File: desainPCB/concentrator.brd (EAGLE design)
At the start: 191.8 x 77.1 mm, 23 parts, among them M1 ARDUINO-PRO-MINI-5.0V, M2 ARDUINO-PRO-MINI-5.0V, M3 ARDUINO-PRO-MINI-5.0V, M4 ARDUINO-PRO-MINI-5.0V

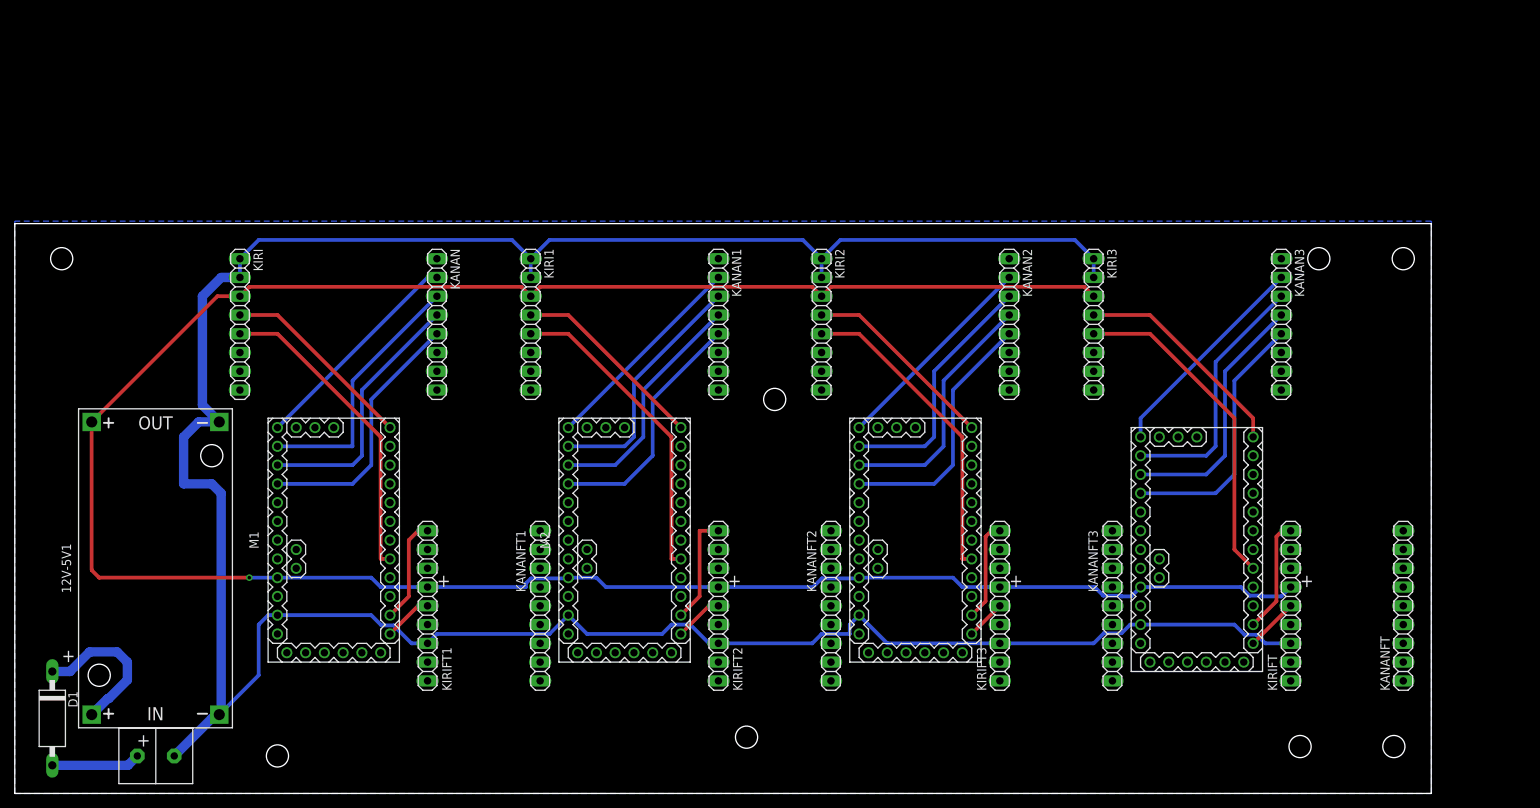
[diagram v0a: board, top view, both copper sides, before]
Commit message: new sensor suhu
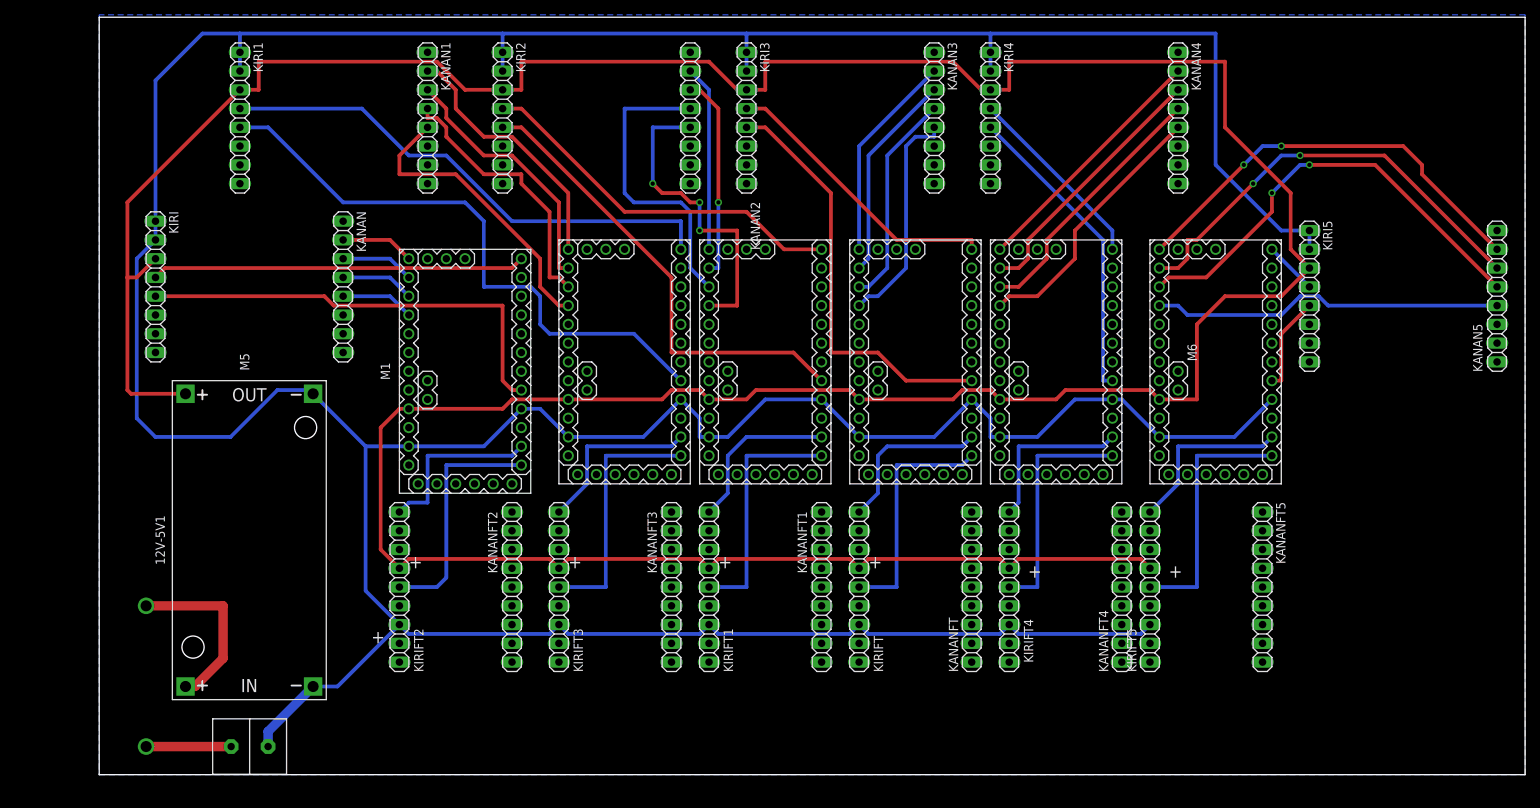
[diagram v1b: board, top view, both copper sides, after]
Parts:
- removed D1: 1N5060GP, diode:DO15-12
- added KANAN4, KANAN5, KIRI4, KIRI5: (no value), pinhead:1X08
- added KANANFT4, KANANFT5, KIRIFT4, KIRIFT5: (no value), pinhead:1X09
- added M5, M6: ARDUINO-PRO-MINI-5.0V, diy-modules:ARDUINO-PRO-MINI
- moved KANANFT3 59.7 mm to (88.9, 27.9)
- moved KIRIFT3 59.7 mm to (73.7, 27.9)
- moved KANANFT 58.5 mm to (129.5, 27.9)
- moved KIRIFT 58.5 mm to (114.3, 27.9)
- moved KIRI3 54.7 mm to (99.1, 91.4)
- moved KANAN3 54.7 mm to (124.5, 91.4)
- moved KANAN2 51.4 mm to (91.4, 91.4)
- moved KIRI2 51.4 mm to (66.0, 91.4)
- moved KANAN1 48.3 mm to (55.9, 91.4)
- moved KIRI1 48.3 mm to (30.5, 91.4)
- moved M4 45.8 mm to (121.9, 58.4)
- moved KIRIFT2 43.3 mm to (52.1, 27.9)
- moved KANANFT2 43.3 mm to (67.3, 27.9)
- moved KIRIFT1 38.2 mm to (94.0, 27.9)
- moved KANANFT1 38.2 mm to (109.2, 27.9)
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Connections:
- removed net 10: KANAN.2, KANAN1.2, KANAN2.2, KANAN3.2, M1.J6.12, M2.J6.12, M3.J6.12, M4.J6.12
- removed net 11: KANAN.3, KANAN1.3, KANAN2.3, KANAN3.3, M1.J6.11, M2.J6.11, M3.J6.11, M4.J6.11
- removed net 12: KANAN.4, KANAN1.4, KANAN2.4, KANAN3.4, M1.J6.10, M2.J6.10, M3.J6.10, M4.J6.10
- removed net 13: KANAN.5, KANAN1.5, KANAN2.5, KANAN3.5, M1.J6.9, M2.J6.9, M3.J6.9, M4.J6.9
- removed net 2: KIRI.5, KIRI1.5, KIRI2.5, KIRI3.5, M1.J7.8, M2.J7.8, M3.J7.8, M4.J7.8
- removed net 4: M2.J7.6
- removed net 9: KIRI.4, KIRI1.4, KIRI2.4, KIRI3.4, M1.J7.1, M2.J7.1, M3.J7.1, M4.J7.1
- removed net D3: M4.J7.7
- removed net GND: 12V-5V1.IN-, 12V-5V1.OUT-, KIRI.1, KIRI.2, KIRI1.1, KIRI1.2, KIRI2.1, KIRI2.2, KIRI3.1, KIRI3.2, KIRIFT.3, KIRIFT1.3, KIRIFT2.3, KIRIFT3.3, M1.J6.2, M2.J6.2, M3.J6.2, M4.J6.2, U$1.P0
- removed net N$1: 12V-5V1.IN+, D1.C
- removed net N$2: D1.A, U$1.P1
- removed net RAW: M1.J6.1, M2.J6.1, M3.J6.1, M4.J6.1
- removed net RXD: KIRIFT.5, KIRIFT1.5, KIRIFT2.5, KIRIFT3.5, M1.J7.12, M2.J7.12, M3.J7.12, M4.J7.12
- removed net TXD: KIRIFT.9, KIRIFT1.9, KIRIFT2.9, KIRIFT3.9, M1.J7.11, M2.J7.11, M3.J7.11, M4.J7.11
- new net 1: M1.J6.1, M2.J6.1, M3.J6.1, M4.J6.1, M5.J6.1, M6.J6.1
- new net 10.1: KANAN.2, M1.J6.12
- new net 10.2: KANAN2.2, M3.J6.12
- new net 10.3: KANAN1.2, M2.J6.12
- new net 10.4: KANAN3.2, M4.J6.12
- new net 10.5: KANAN4.2, M5.J6.12
- new net 10.6: KANAN5.2, M6.J6.12
- new net 11.1: KANAN.3, M1.J6.11
- new net 11.2: KANAN2.3, M3.J6.11
- new net 11.3: KANAN1.3, M2.J6.11
- new net 11.4: KANAN3.3, M4.J6.11
- new net 11.5: KANAN4.3, M5.J6.11
- new net 11.6: KANAN5.3, M6.J6.11
- new net 12.1: KANAN.4, M1.J6.10
- new net 12.2: KANAN2.4, M3.J6.10
- new net 12.3: KANAN1.4, M2.J6.10
- new net 12.4: KANAN3.4, M4.J6.10
- new net 12.5: KANAN4.4, M5.J6.10
- new net 12.6: KANAN5.4, M6.J6.10
- new net 13.1: KANAN.5, M1.J6.9
- new net 13.2: KANAN2.5, M3.J6.9
- new net 13.3: KANAN1.5, M2.J6.9
- new net 13.4: KANAN3.5, M4.J6.9
- new net 13.5: KANAN4.5, M5.J6.9
- new net 13.6: KANAN5.5, M6.J6.9
- new net 2.1: KIRI.5, M1.J7.8
- new net 2.2: KIRI2.5, M3.J7.8
- new net 2.3: KIRI1.5, M2.J7.8
- new net 2.4: KIRI3.5, M4.J7.8
- new net 2.5: KIRI4.5, M5.J7.8
- new net 2.6: KIRI5.5, M6.J7.8
- new net 4.5: M5.J7.6
- new net 8.5: M5.J7.2
- new net 9.1: KIRI.4, M1.J7.1
- new net 9.2: KIRI2.4, M3.J7.1
- new net 9.3: KIRI1.4, M2.J7.1
- new net 9.4: KIRI3.4, M4.J7.1
- new net 9.5: KIRI4.4, M5.J7.1
- new net 9.6: KIRI5.4, M6.J7.1
- new net IN+: U$1.P1
- new net OUT+: 12V-5V1.IN+
- new net RXD.1: KIRIFT2.5, M1.J7.12
- new net RXD.2: KIRIFT1.5, M3.J7.12
- new net RXD.3: KIRIFT3.5, M2.J7.12
- new net RXD.4: KIRIFT.5, M4.J7.12
- new net RXD.5: KIRIFT4.5, M5.J7.12
- new net RXD6: KIRIFT5.5, M6.J7.12
- new net TXD.1: KIRIFT2.9, M1.J7.11
- new net TXD.2: KIRIFT1.9, M3.J7.11
- new net TXD.3: KIRIFT3.9, M2.J7.11
- new net TXD.4: KIRIFT.9, M4.J7.11
- new net TXD.5: KIRIFT4.9, M5.J7.11
- new net TXD6: KIRIFT5.9, M6.J7.11
- net 3V: now also KIRI4.3, KIRI5.3, KIRIFT4.6, KIRIFT5.6, M5.J6.4, M6.J6.4
- net 8: no longer M2.J7.2
- net GND.1: now also 12V-5V1.IN-, 12V-5V1.OUT-, KIRI.1, KIRI.2, KIRI1.1, KIRI1.2, KIRI2.1, KIRI2.2, KIRI3.1, KIRI3.2, KIRI4.1, KIRI4.2, KIRI5.1, KIRI5.2, KIRIFT.3, KIRIFT1.3, KIRIFT2.3, KIRIFT3.3, KIRIFT4.3, KIRIFT5.3, M1.J6.2, M2.J6.2, M3.J6.2, M4.J6.2, M5.J6.2, M5.J7.9, M6.J6.2, M6.J7.9, U$1.P0
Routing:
- net GND.1: track 0.00 -> 595.4 mm
- net GND: track 379.1 -> 0.00 mm
- net 3V: track 333.7 -> 517.7 mm, vias 1 -> 0
- net 2: track 173.0 -> 0.00 mm
- net 13: track 138.5 -> 0.00 mm
- net 11: track 137.0 -> 0.00 mm
- net 12: track 136.3 -> 0.00 mm
- net 10: track 117.0 -> 0.00 mm
- net 9: track 109.8 -> 0.00 mm
- net 2.3: track 0.00 -> 81.3 mm
- net 9.3: track 0.00 -> 69.8 mm
- net 2.2: track 0.00 -> 63.3 mm
- net 12.6: track 0.00 -> 60.9 mm, vias 0 -> 2
- net 2.1: track 0.00 -> 60.7 mm
- net 11.6: track 0.00 -> 59.8 mm, vias 0 -> 2
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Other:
- board size 191.8 x 77.1 mm -> 193 x 102.5 mm
